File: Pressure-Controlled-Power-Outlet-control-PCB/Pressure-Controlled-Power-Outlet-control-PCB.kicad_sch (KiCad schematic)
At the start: 31 parts, among them J1 Analog water pressure sensor 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, J2 1017514, J3 I2C0 Connector, J4 SPI1 Connector, K1 T9GV5L24-24, K2 T9GV5L24-24, Q1 2N3906, Q2 IRF540N, Q3 IRF540N, Q4 2N3906, U1 Pico, U2 LM324, U3 LF50_TO220

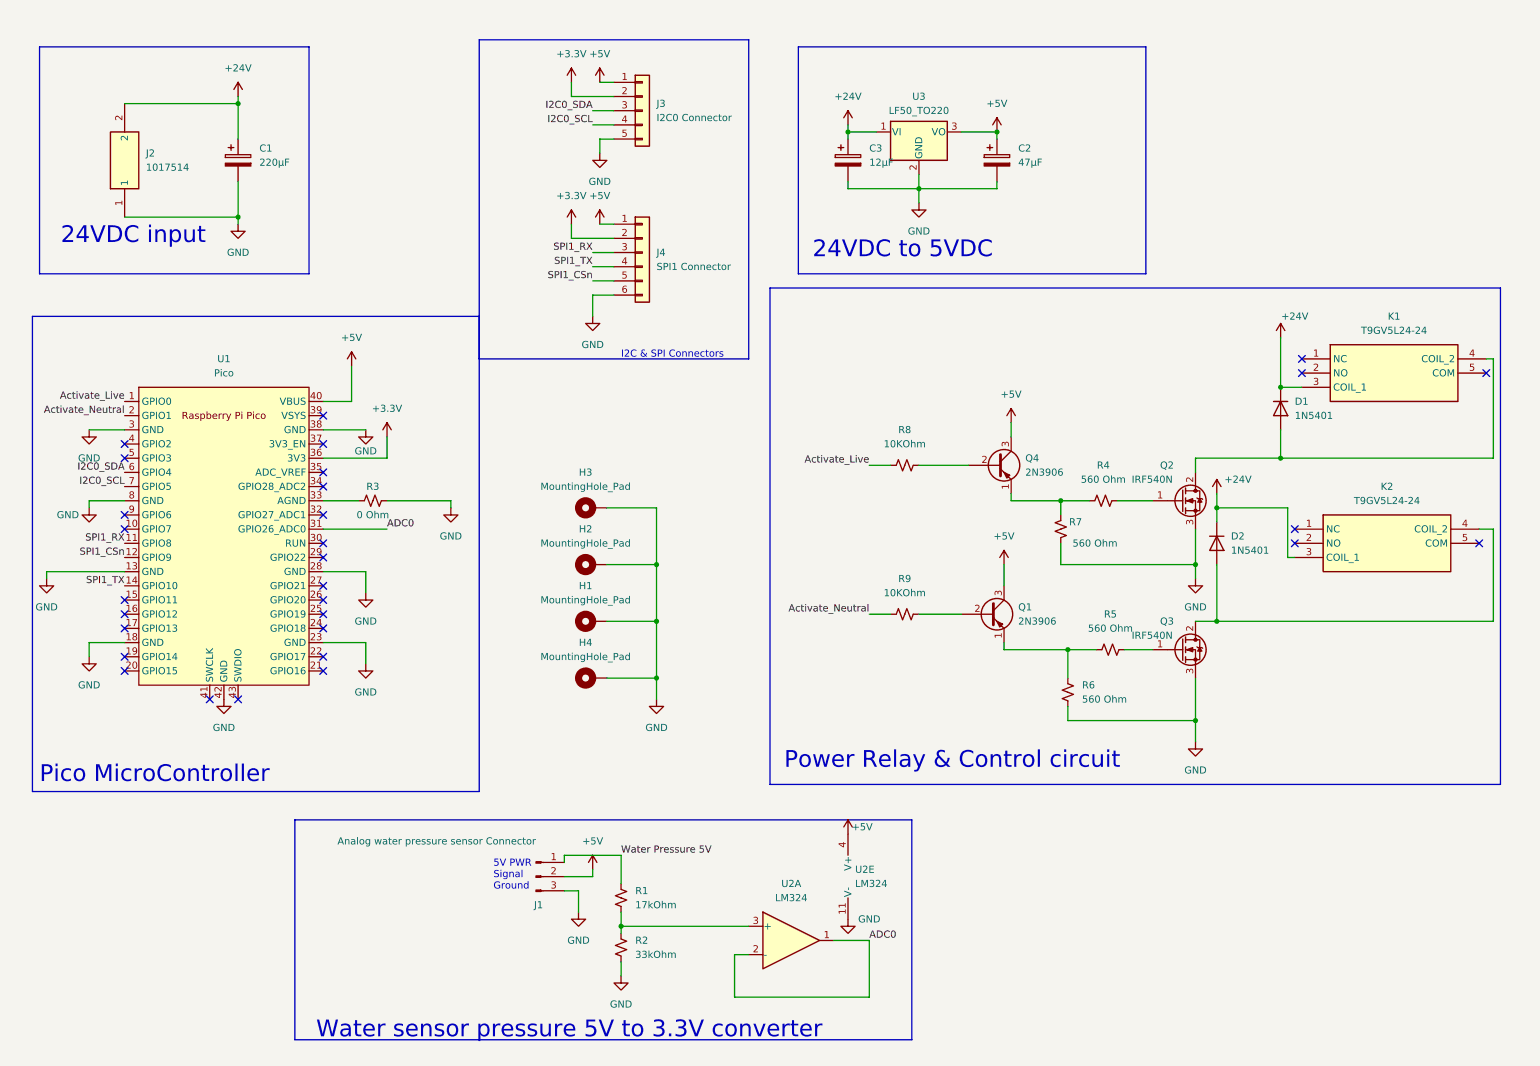
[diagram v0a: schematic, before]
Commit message: sign a new feature creep added two fan headers that can power ether 24 or 5 volt fans
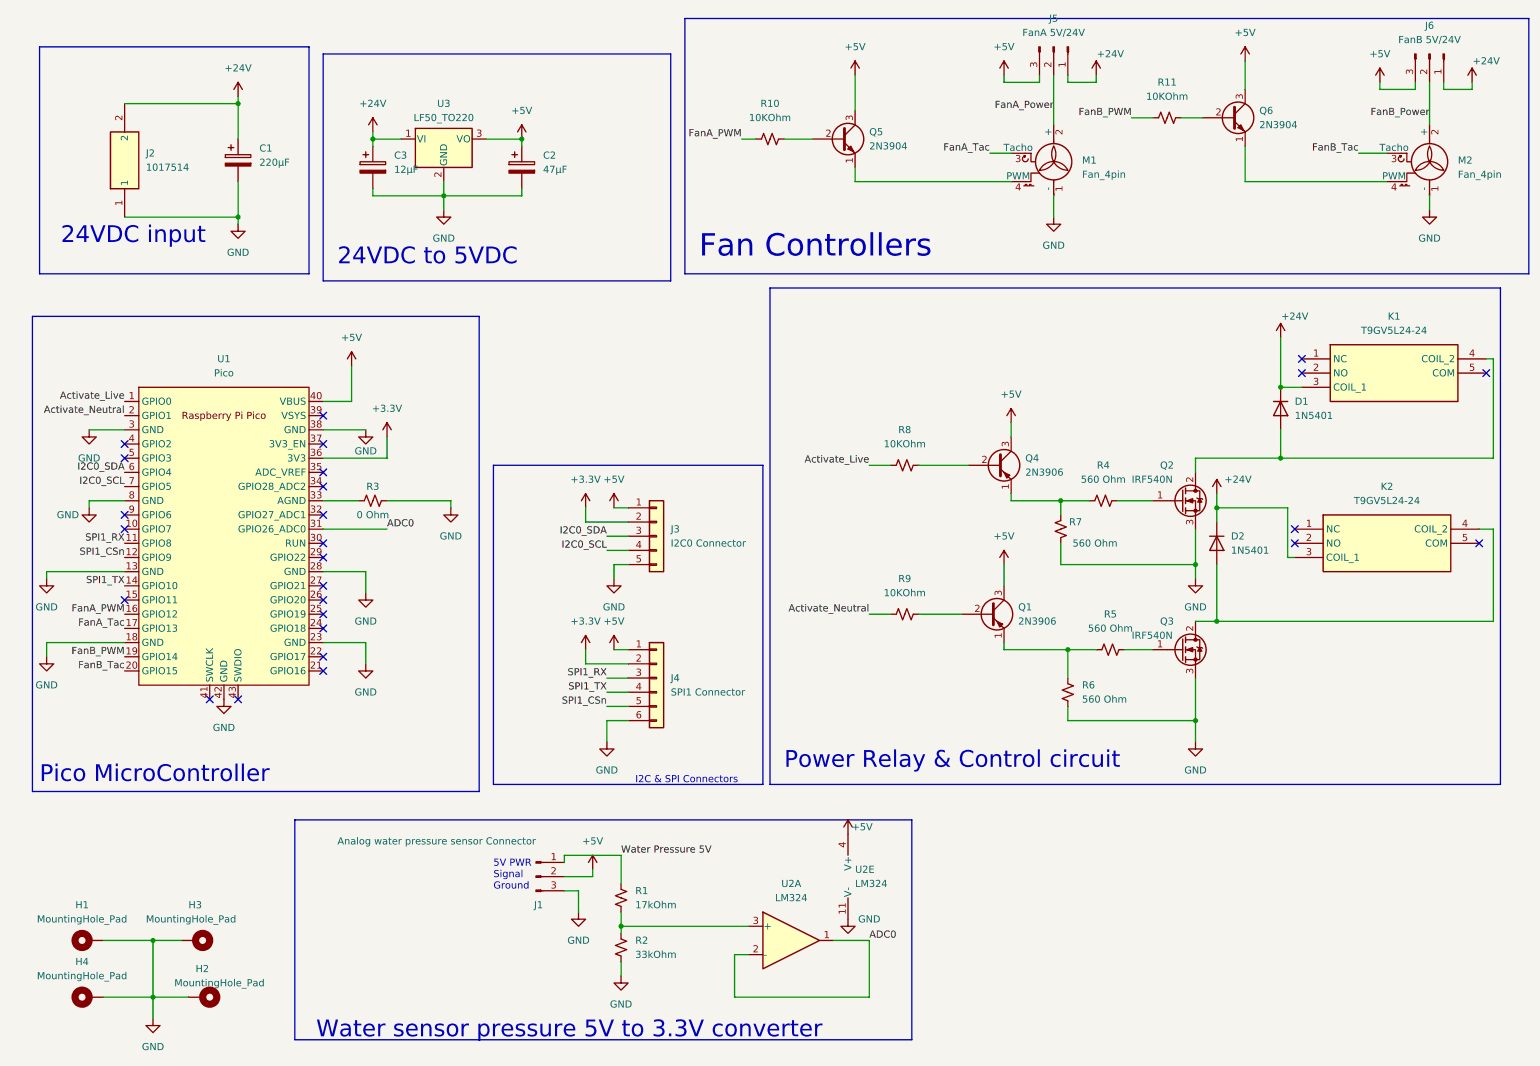
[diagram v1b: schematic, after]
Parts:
- added J5: FanA 5V/24V, Connector_PinHeader_2.54mm:PinHeader_1x03_P2.54mm_Vertical, symbol Connector:Conn_01x03_Pin
- added J6: FanB 5V/24V, Connector_PinHeader_2.54mm:PinHeader_1x03_P2.54mm_Vertical, symbol Connector:Conn_01x03_Pin
- added M1, M2: Fan_4pin, Connector:FanPinHeader_1x04_P2.54mm_Vertical, symbol Motor:Fan_4pin
- added Q5, Q6: 2N3904, Package_TO_SOT_THT:TO-92_Inline, symbol Transistor_BJT:2N3904
- added R10, R11: 10KOhm, Resistor_THT:R_Axial_DIN0207_L6.3mm_D2.5mm_P2.54mm_Vertical, symbol Device:R_Small_US
- J1: footprint Connector_PinSocket_2.54mm:PinSocket_1x03_P2.54mm_Vertical -> Connector_PinHeader_2.54mm:PinHeader_1x03_P2.54mm_Vertical
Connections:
- net +24V: now also J5.1 (Pin_1), J6.1 (Pin_1)
- net +5V: now also J5.3 (Pin_3), J6.3 (Pin_3), Q5.3 (C), Q6.3 (C)
- net GND: now also M1.1 (-), M2.1 (-)
- net FanA_PWM: now reaches U1.16 (GPIO12)
- net FanA_PWM: now also R10.1
- net FanA_Tac: now reaches U1.17 (GPIO13)
- net FanA_Tac: now also M1.3 (Tacho)
- net FanB_PWM: now reaches U1.19 (GPIO14)
- net FanB_PWM: now also R11.1
- net FanB_Tac: now reaches U1.20 (GPIO15)
- net FanB_Tac: now also M2.3 (Tacho)
- new net: M1.4 (PWM), Q5.1 (E)
- new net: Q5.2 (B), R10.2
- new net: Q6.2 (B), R11.2
- new net: M2.4 (PWM), Q6.1 (E)
- new net FanA_Power: J5.2 (Pin_2), M1.2 (+)
- new net FanB_Power: J6.2 (Pin_2), M2.2 (+)
- no-connect marks 30 -> 26
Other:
- note added: "Fan Controllers"
- moved on the sheet: C2, C3, H1, H2, H3, H4, J3, J4, U3

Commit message: Added name
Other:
- note added: "Screw mounting holes"
- company: (none) -> Brian
- moved on the sheet: H1, H2, H3, H4
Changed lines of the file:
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@@
     (title "Pressure Controlled Power Outlet")
     (date "2024-07-18")
-    (rev "V1.1.1")
+    (rev "V1.2.2")
+    (company "Brian")
   )
   (junction (at 121.92 175.26) (diameter 0) (color 0 0 0 0)
   )
-  (junction (at 38.1 177.8) (diameter 0) (color 0 0 0 0)
+  (junction (at 40.64 171.45) (diameter 0) (color 0 0 0 0)
   )
   (junction (at 201.93 125.73) (diameter 0) (color 0 0 0 0)
@@
   (junction (at 77.47 34.29) (diameter 0) (color 0 0 0 0)
   )
-  (junction (at 38.1 187.96) (diameter 0) (color 0 0 0 0)
+  (junction (at 40.64 181.61) (diameter 0) (color 0 0 0 0)
   )
   (junction (at 53.34 27.94) (diameter 0) (color 0 0 0 0)
@@
     (stroke (width 0) (type default))
   )
-  (wire (pts (xy 38.1 177.8) (xy 43.18 177.8))
+  (wire (pts (xy 40.64 171.45) (xy 45.72 171.45))
     (stroke (width 0) (type default))
   )
@@
     (stroke (width 0) (type default))
   )
-  (wire (pts (xy 29.21 187.96) (xy 38.1 187.96))
+  (wire (pts (xy 31.75 181.61) (xy 40.64 181.61))
     (stroke (width 0) (type default))
   )
@@
     (stroke (width 0) (type default))
   )
-  (wire (pts (xy 38.1 191.77) (xy 38.1 187.96))
+  (wire (pts (xy 40.64 185.42) (xy 40.64 181.61))
     (stroke (width 0) (type default))
   )
@@
     (stroke (width 0) (type default))
   )
-  (wire (pts (xy 38.1 187.96) (xy 38.1 177.8))
+  (wire (pts (xy 40.64 181.61) (xy 40.64 171.45))
     (stroke (width 0) (type default))
   )
@@
     (stroke (width 0) (type default))
   )
-  (wire (pts (xy 29.21 177.8) (xy 38.1 177.8))
+  (wire (pts (xy 31.75 171.45) (xy 40.64 171.45))
     (stroke (width 0) (type default))
   )
@@
     (stroke (width 0) (type default))
   )
-  (wire (pts (xy 44.45 187.96) (xy 38.1 187.96))
+  (wire (pts (xy 46.99 181.61) (xy 40.64 181.61))
     (stroke (width 0) (type default))
   )
@@
     (fill (type none))
   )
+  (rectangle (start 15.24 157.48) (end 62.23 195.58)
+    (stroke (width 0) (type default))
+    (fill (type none))
+  )
   (rectangle (start 63.5 156.21) (end 173.99 195.58)
     (stroke (width 0) (type default))
@@
     (stroke (width 0) (type default))
     (fill (type none))
+  )
+  (text "Screw mounting holes" (at 17.78 194.31 0)
+    (effects (font (size 1.27 1.27)) (justify left bottom))
   )
   (text "24VDC input" (at 21.59 53.34 0)
@@
     )
   )
-  (symbol (lib_id "Mechanical:MountingHole_Pad") (at 26.67 177.8 90) (unit 1)
-    (in_bom yes) (on_board yes) (dnp no) (fields_autoplaced)
-    (property "Reference" "H1" (at 25.4 171.45 90)
-      (effects (font (size 1.27 1.27)))
-    )
-    (property "Value" "MountingHole_Pad" (at 25.4 173.99 90)
-      (effects (font (size 1.27 1.27)))
-    )
-    (property "Footprint" "MountingHole:MountingHole_2.2mm_M2_Pad" (at 26.67 177.8 0)
-      (effects (font (size 1.27 1.27)) hide)
-    )
-    (property "Datasheet" "~" (at 26.67 177.8 0)
+  (symbol (lib_id "Mechanical:MountingHole_Pad") (at 29.21 171.45 90) (unit 1)
+    (in_bom yes) (on_board yes) (dnp no) (fields_autoplaced)
+    (property "Reference" "H1" (at 27.94 165.1 90)
+      (effects (font (size 1.27 1.27)))
+    )
+    (property "Value" "MountingHole_Pad" (at 27.94 167.64 90)
+      (effects (font (size 1.27 1.27)))
+    )
+    (property "Footprint" "MountingHole:MountingHole_2.2mm_M2_Pad" (at 29.21 171.45 0)
+      (effects (font (size 1.27 1.27)) hide)
+    )
+    (property "Datasheet" "~" (at 29.21 171.45 0)
       (effects (font (size 1.27 1.27)) hide)
     )
@@
     )
   )
-  (symbol (lib_id "Mechanical:MountingHole_Pad") (at 45.72 177.8 270) (unit 1)
+  (symbol (lib_id "Mechanical:MountingHole_Pad") (at 48.26 171.45 270) (unit 1)
     (in_bom yes) (on_board yes) (dnp no)
-    (property "Reference" "H3" (at 44.45 171.45 90)
-      (effects (font (size 1.27 1.27)) (justify left))
-    )
-    (property "Value" "MountingHole_Pad" (at 36.83 173.99 90)
-      (effects (font (size 1.27 1.27)) (justify left))
-    )
-    (property "Footprint" "MountingHole:MountingHole_2.2mm_M2_Pad" (at 45.72 177.8 0)
-      (effects (font (size 1.27 1.27)) hide)
-    )
-    (property "Datasheet" "~" (at 45.72 177.8 0)
+    (property "Reference" "H3" (at 46.99 165.1 90)
+      (effects (font (size 1.27 1.27)) (justify left))
+    )
+    (property "Value" "MountingHole_Pad" (at 39.37 167.64 90)
+      (effects (font (size 1.27 1.27)) (justify left))
+    )
+    (property "Footprint" "MountingHole:MountingHole_2.2mm_M2_Pad" (at 48.26 171.45 0)
+      (effects (font (size 1.27 1.27)) hide)
+    )
+    (property "Datasheet" "~" (at 48.26 171.45 0)
       (effects (font (size 1.27 1.27)) hide)
     )
@@
     )
   )
-  (symbol (lib_id "power:GND") (at 38.1 191.77 0) (unit 1)
-    (in_bom yes) (on_board yes) (dnp no) (fields_autoplaced)
-    (property "Reference" "#PWR027" (at 38.1 198.12 0)
-      (effects (font (size 1.27 1.27)) hide)
-    )
-    (property "Value" "GND" (at 38.1 196.85 0)
-      (effects (font (size 1.27 1.27)))
-    )
-    (property "Footprint" "" (at 38.1 191.77 0)
-      (effects (font (size 1.27 1.27)) hide)
-    )
-    (property "Datasheet" "" (at 38.1 191.77 0)
+  (symbol (lib_id "power:GND") (at 40.64 185.42 0) (unit 1)
+    (in_bom yes) (on_board yes) (dnp no) (fields_autoplaced)
+    (property "Reference" "#PWR027" (at 40.64 191.77 0)
+      (effects (font (size 1.27 1.27)) hide)
+    )
+    (property "Value" "GND" (at 40.64 190.5 0)
+      (effects (font (size 1.27 1.27)))
+    )
+    (property "Footprint" "" (at 40.64 185.42 0)
+      (effects (font (size 1.27 1.27)) hide)
+    )
+    (property "Datasheet" "" (at 40.64 185.42 0)
       (effects (font (size 1.27 1.27)) hide)
     )
@@
     )
   )
-  (symbol (lib_id "Mechanical:MountingHole_Pad") (at 46.99 187.96 270) (unit 1)
+  (symbol (lib_id "Mechanical:MountingHole_Pad") (at 49.53 181.61 270) (unit 1)
     (in_bom yes) (on_board yes) (dnp no)
-    (property "Reference" "H2" (at 45.72 182.88 90)
-      (effects (font (size 1.27 1.27)) (justify left))
-    )
-    (property "Value" "MountingHole_Pad" (at 41.91 185.42 90)
-      (effects (font (size 1.27 1.27)) (justify left))
-    )
-    (property "Footprint" "MountingHole:MountingHole_2.2mm_M2_Pad" (at 46.99 187.96 0)
-      (effects (font (size 1.27 1.27)) hide)
-    )
-    (property "Datasheet" "~" (at 46.99 187.96 0)
+    (property "Reference" "H2" (at 48.26 176.53 90)
+      (effects (font (size 1.27 1.27)) (justify left))
+    )
+    (property "Value" "MountingHole_Pad" (at 44.45 179.07 90)
+      (effects (font (size 1.27 1.27)) (justify left))
+    )
+    (property "Footprint" "MountingHole:MountingHole_2.2mm_M2_Pad" (at 49.53 181.61 0)
+      (effects (font (size 1.27 1.27)) hide)
+    )
+    (property "Datasheet" "~" (at 49.53 181.61 0)
       (effects (font (size 1.27 1.27)) hide)
     )
@@
     )
   )
-  (symbol (lib_id "Mechanical:MountingHole_Pad") (at 26.67 187.96 90) (unit 1)
-    (in_bom yes) (on_board yes) (dnp no) (fields_autoplaced)
-    (property "Reference" "H4" (at 25.4 181.61 90)
-      (effects (font (size 1.27 1.27)))
-    )
-    (property "Value" "MountingHole_Pad" (at 25.4 184.15 90)
-      (effects (font (size 1.27 1.27)))
-    )
-    (property "Footprint" "MountingHole:MountingHole_2.2mm_M2_Pad" (at 26.67 187.96 0)
-      (effects (font (size 1.27 1.27)) hide)
-    )
-    (property "Datasheet" "~" (at 26.67 187.96 0)
-      (effects (font (size 1.27 1.27)) hide)
-    )
+  (symbol (lib_id "Mechanical:MountingHole_Pad") (at 29.21 181.61 90) (unit 1)
+    (in_bom yes) (on_board yes) (dnp no) (fields_autoplaced)
+    (property "Reference" "H4" (at 27.94 175.26 90)
+      (effects (font (size 1.27 1.27)))
+    )
+    (property "Value" "MountingHole_Pad" (at 27.94 177.8 90)
+      (effects (font (size 1.27 1.27)))
+    )
+    (property "Footprint" "MountingHole:MountingHole_2.2mm_M2_Pad" (at 29.21 181.61 0)
+      (effects (font (size 1.27 1.27)) hide)
+    )
+    (property "Datasheet" "~" (at 29.21 181.61 0)
+      (effects (font (size 1.27 1.27)) hide)
+    )

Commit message: added name to pcb
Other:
- company: Brian -> Brian Banas
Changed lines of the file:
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@@
     (title "Pressure Controlled Power Outlet")
     (date "2024-07-18")
-    (rev "V1.2.2")
-    (company "Brian")
+    (rev "V1.2.3")
+    (company "Brian Banas")
   )
   (junction (at 121.92 175.26) (diameter 0) (color 0 0 0 0)

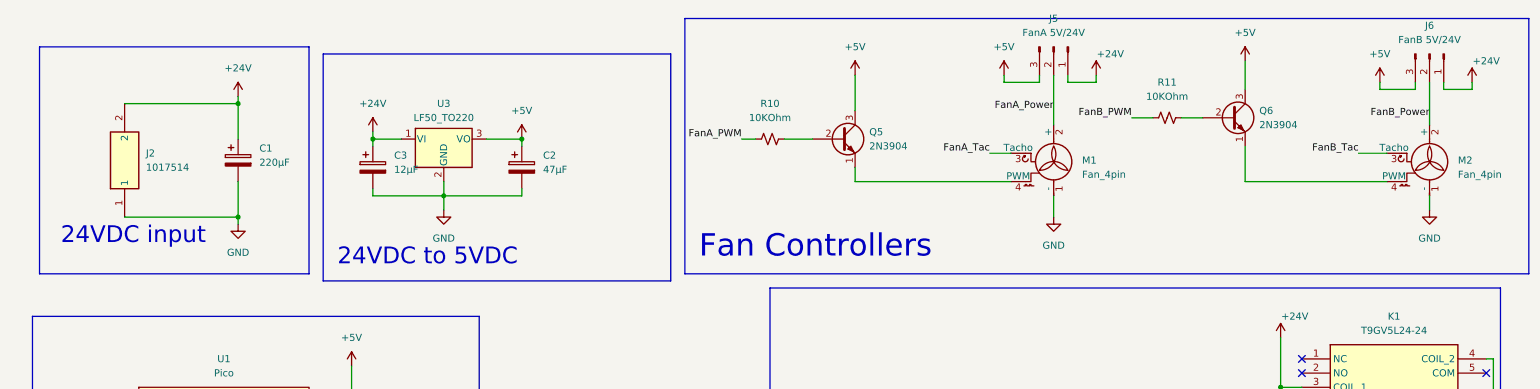
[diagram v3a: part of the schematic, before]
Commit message: redid the fan controllers
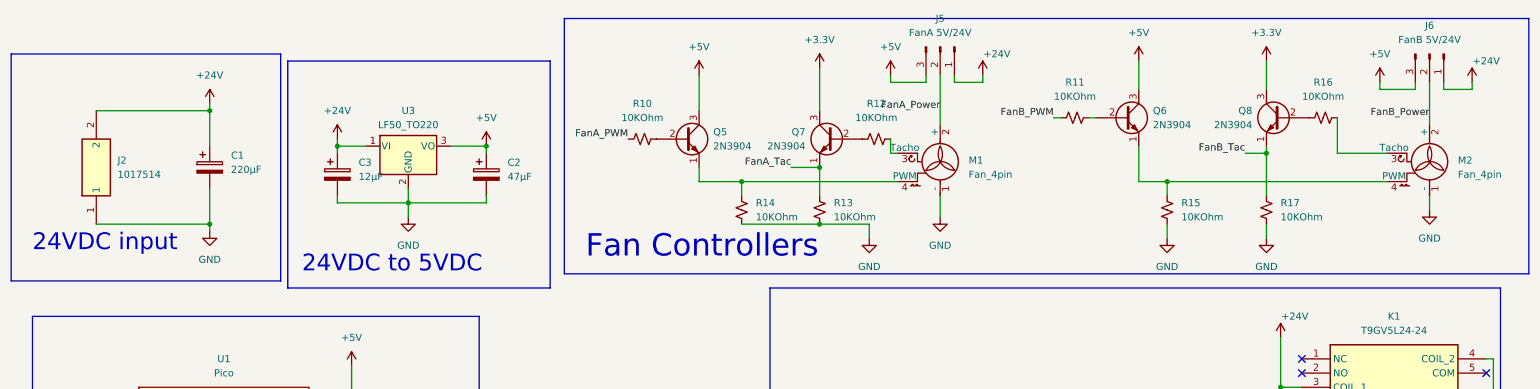
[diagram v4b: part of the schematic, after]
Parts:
- added Q7, Q8: 2N3904, Package_TO_SOT_THT:TO-92_Inline, symbol Transistor_BJT:2N3904
- added R12, R13, R14, R15, R16, R17: 10KOhm, Resistor_THT:R_Axial_DIN0207_L6.3mm_D2.5mm_P2.54mm_Vertical, symbol Device:R_Small_US
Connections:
- net +3.3V: now also Q7.3 (C), Q8.3 (C)
- net FanA_Tac: now also Q7.1 (E), R13.2; no longer M1.3 (Tacho)
- net FanB_Tac: now also Q8.1 (E), R17.2; no longer M2.3 (Tacho)
- net GND: now also R13.1, R14.1, R15.1, R17.1
- net at M1.4 (PWM), Q5.1 (E): now also R14.2
- net at M2.4 (PWM), Q6.1 (E): now also R15.2
- new net: Q8.2 (B), R16.1
- new net: M2.3 (Tacho), R16.2
- new net: M1.3 (Tacho), R12.2
- new net: Q7.2 (B), R12.1
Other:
- moved on the sheet: C1, C2, C3, J2, J5, M1, Q5, Q6, R10, R11, U3
